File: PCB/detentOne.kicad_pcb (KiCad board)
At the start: 2 copper layers, 150 x 85 mm, 88 parts, among them J1 Conn_01x07, J2 Conn_01x03, SW1 SW_Push, SW2 SW_Push, SW3 SW_Push, SW4 SW_Push, SW5 SW_Push, SW6 SW_Push, SW7 C92589, SW8 C92589, U2 SGM2050XTRL20G/TR, U3 ESP32-S3-WROOM-1(N16R8), U4 TMC6300-LA-T_C5274455, U5 XY-GH1.25-7A61, U6 PCA9554ARGVR, U7 AS5047P-ATSM_C962063

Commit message: PCB schematic checked - ready to trace
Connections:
- C10 pad 1: VBAT -> 5V
- C12 pad 1: VBAT -> 5V
- C4 pad 2: /PowerManagement/5V -> 5V
- C9 pad 1: VBAT -> 5V
- D5 pad 1: USB_D+ -> USB_D+_UP
- D5 pad 3: USB_D- -> USB_D-_UP
- U2 pad 14: /PowerManagement/5V -> 5V
- U2 pad 15: /PowerManagement/5V -> 5V
- U2 pad 16: /PowerManagement/5V -> 5V
- U2 pad 17: /PowerManagement/5V -> 5V
- U4 pad 18: VBAT -> 5V
- USB1 pad 11: /PowerManagement/5V -> 5V
- USB1 pad 2: /PowerManagement/5V -> 5V
- USB1 pad 5: USB_D- -> USB_D-_UP
- USB1 pad 6: USB_D+ -> USB_D+_UP
- USB1 pad 7: USB_D- -> USB_D-_UP
- USB1 pad 8: USB_D+ -> USB_D+_UP
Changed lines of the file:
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@@
 	)
 	(net 0 "")
-	(net 1 "/PowerManagement/5V")
+	(net 1 "5V")
 	(net 2 "GND")
-	(net 3 "VBAT")
+	(net 3 "USB_D+_UP")
 	(net 4 "3V3")
 	(net 5 "Net-(U2-NR{slash}SS)")
@@
 	(net 95 "Net-(LED16-DOUT)")
 	(net 96 "unconnected-(LED17-DOUT-Pad2)")
+	(net 97 "USB_D-_UP")
 	(footprint "MountingHole:MountingHole_2.2mm_M2"
 		(layer "F.Cu")
@@
 			(layers "F.Cu" "F.Mask" "F.Paste")
 			(roundrect_rratio 0.25)
-			(net 3 "VBAT")
+			(net 1 "5V")
 			(pintype "passive")
 		)
@@
 			(layers "F.Cu" "F.Mask" "F.Paste")
 			(roundrect_rratio 0.25)
-			(net 3 "VBAT")
+			(net 1 "5V")
 			(pintype "passive")
 		)
@@
 			(size 0.55 1.1)
 			(layers "F.Cu" "F.Mask" "F.Paste")
-			(net 1 "/PowerManagement/5V")
+			(net 1 "5V")
 			(pinfunction "VBUS")
 			(pintype "unspecified")
@@
 			(size 0.3 1.1)
 			(layers "F.Cu" "F.Mask" "F.Paste")
-			(net 16 "USB_D-")
+			(net 97 "USB_D-_UP")
 			(pinfunction "DN2")
 			(pintype "unspecified")
@@
 			(size 0.3 1.1)
 			(layers "F.Cu" "F.Mask" "F.Paste")
-			(net 15 "USB_D+")
+			(net 3 "USB_D+_UP")
 			(pinfunction "DP1")
 			(pintype "unspecified")
@@
 			(size 0.3 1.1)
 			(layers "F.Cu" "F.Mask" "F.Paste")
-			(net 16 "USB_D-")
+			(net 97 "USB_D-_UP")
 			(pinfunction "DN1")
 			(pintype "unspecified")
@@
 			(size 0.3 1.1)
 			(layers "F.Cu" "F.Mask" "F.Paste")
-			(net 15 "USB_D+")
+			(net 3 "USB_D+_UP")
 			(pinfunction "DP2")
 			(pintype "unspecified")
@@
 			(size 0.55 1.1)
 			(layers "F.Cu" "F.Mask" "F.Paste")
-			(net 1 "/PowerManagement/5V")
+			(net 1 "5V")
 			(pinfunction "VBUS")
 			(pintype "unspecified")
@@
 			(size 0.53 1.07)
 			(layers "F.Cu" "F.Mask" "F.Paste")
-			(net 15 "USB_D+")
+			(net 3 "USB_D+_UP")
 			(pinfunction "1")
 			(pintype "input")
@@
 			(size 0.53 1.07)
 			(layers "F.Cu" "F.Mask" "F.Paste")
-			(net 16 "USB_D-")
+			(net 97 "USB_D-_UP")
 			(pinfunction "3")
 			(pintype "input")
@@
 			(layers "F.Cu" "F.Mask" "F.Paste")
 			(roundrect_rratio 0.25)
-			(net 1 "/PowerManagement/5V")
+			(net 1 "5V")
 			(pintype "passive")
 		)
@@
 			(size 0.66 0.2)
 			(layers "F.Cu" "F.Mask" "F.Paste")
-			(net 3 "VBAT")
+			(net 1 "5V")
 			(pinfunction "VS")
 			(pintype "unspecified")
@@
 			(size 0.28 0.8)
 			(layers "F.Cu" "F.Mask" "F.Paste")
-			(net 1 "/PowerManagement/5V")
+			(net 1 "5V")
 			(pinfunction "EN")
 			(pintype "unspecified")
@@
 			(size 0.28 0.8)
 			(layers "F.Cu" "F.Mask" "F.Paste")
-			(net 1 "/PowerManagement/5V")
+			(net 1 "5V")
 			(pinfunction "IN")
 			(pintype "unspecified")
@@
 			(size 0.8 0.28)
 			(layers "F.Cu" "F.Mask" "F.Paste")
-			(net 1 "/PowerManagement/5V")
+			(net 1 "5V")
 			(pinfunction "IN")
 			(pintype "unspecified")
@@
 			(size 0.8 0.28)
 			(layers "F.Cu" "F.Mask" "F.Paste")
-			(net 1 "/PowerManagement/5V")
+			(net 1 "5V")
 			(pinfunction "IN")
 			(pintype "unspecified")
@@
 			(layers "F.Cu" "F.Mask" "F.Paste")
 			(roundrect_rratio 0.25)
-			(net 3 "VBAT")
+			(net 1 "5V")
 			(pintype "passive")
 		)

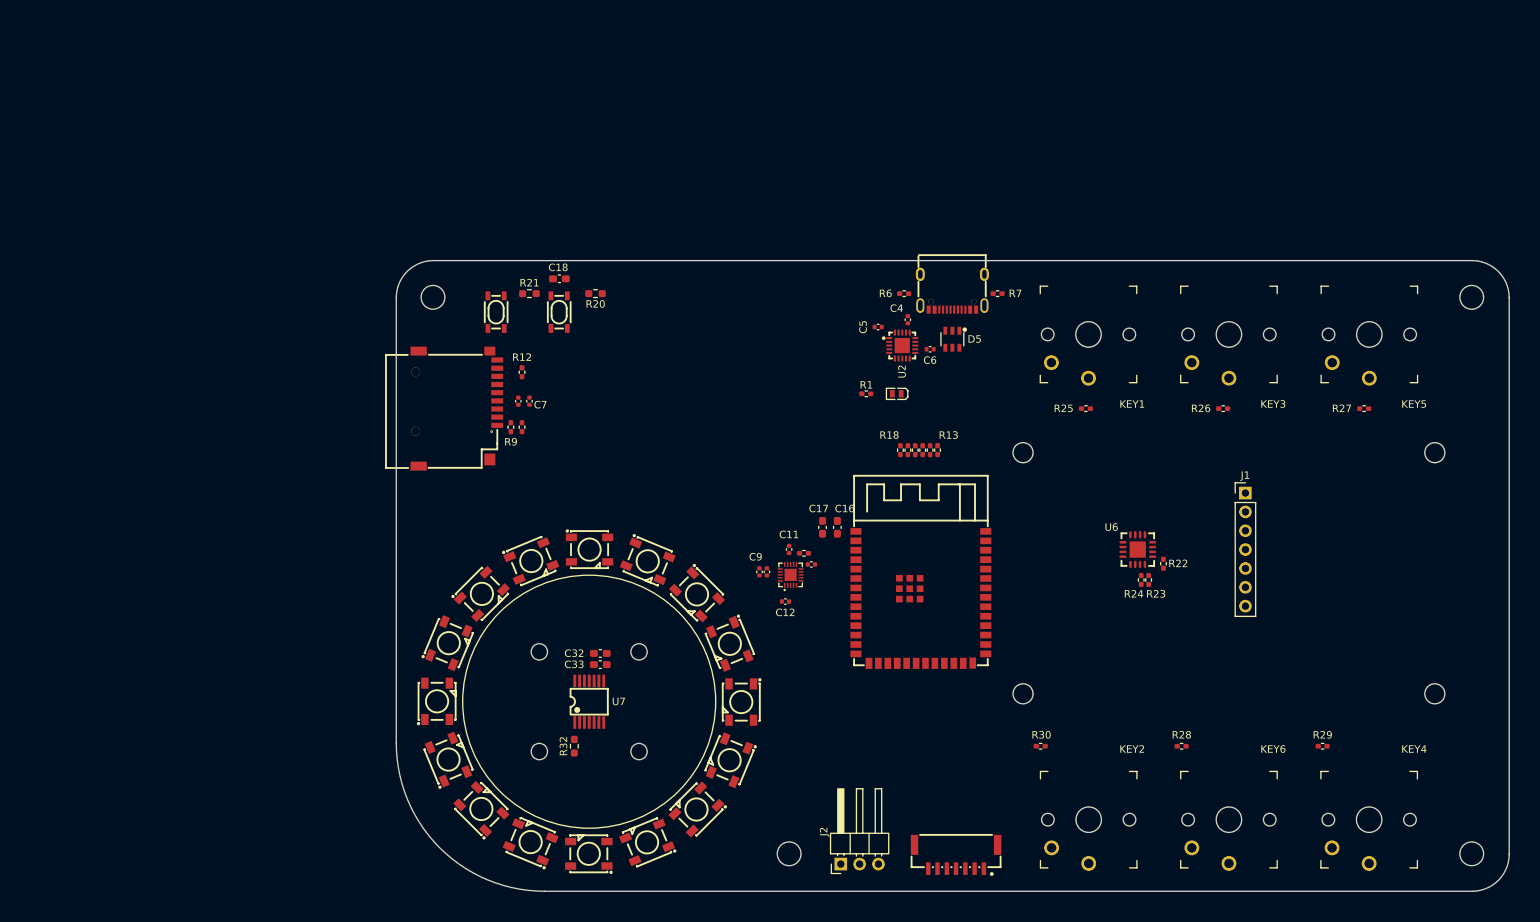
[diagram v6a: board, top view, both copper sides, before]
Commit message: encoder and spi left to trace
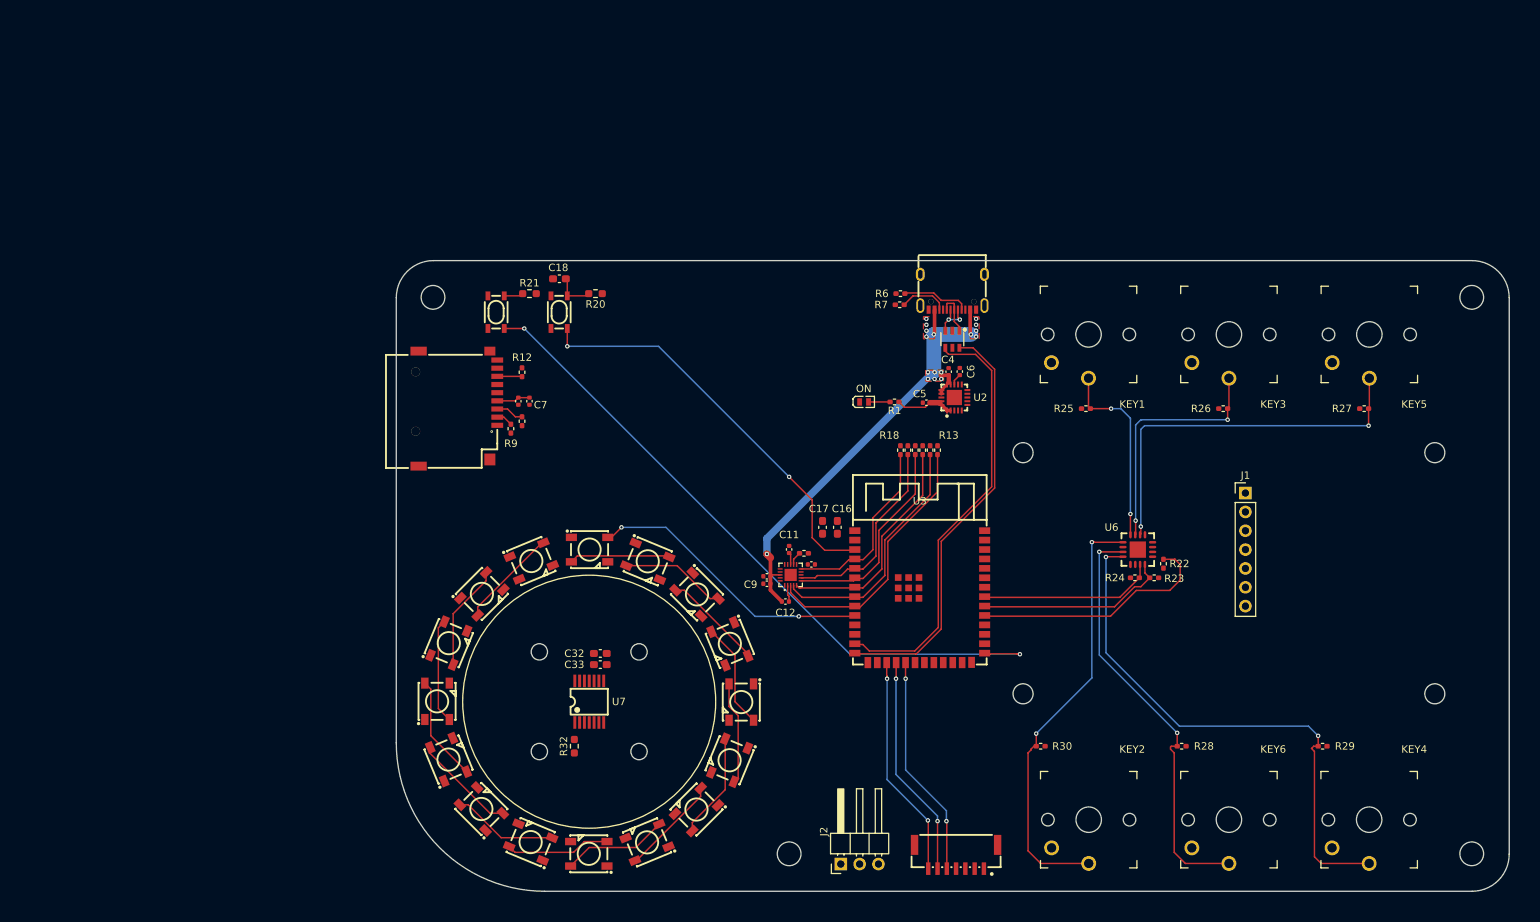
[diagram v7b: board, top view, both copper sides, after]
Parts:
- moved R7 13.3 mm to (151.9, 57.5), turned to 180 degrees
- moved C5 12.1 mm to (155.5, 70.7)
- moved U2 9.91 mm to (159.3, 70.0), turned to 0 degrees
- moved C4 8.90 mm to (158.5, 66.5)
- moved C6 5.00 mm to (160.0, 66.5), turned to -90 degrees
- moved LED1 4.53 mm to (147.1, 70.6), turned to 0 degrees
- moved R1 3.96 mm to (151.2, 70.6), turned to 180 degrees
- moved C9 1.89 mm to (134.0, 95.1), turned to 180 degrees
- moved R24 0.90 mm to (183.6, 94.3), turned to 180 degrees
- moved R23 0.81 mm to (186.2, 94.3), turned to 0 degrees
- moved R10 0.80 mm to (101.0, 73.2)
- moved C10 0.60 mm to (134.0, 94.1), turned to 180 degrees
- moved R6 0.50 mm to (152.0, 56.0)
- moved R9 0.20 mm to (99.5, 74.2)
- moved U3 0.18 mm to (154.6, 96.8)
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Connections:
- U3 pad 10: A_OUT -> NEOPIXEL_DIN
- U3 pad 11: B_OUT -> A_OUT
- U3 pad 12: CURRENT_SENSE -> B_OUT
- U3 pad 17: OLED_DC -> OLED_RST
- U3 pad 18: OLED_RST -> OLED_DC
- U3 pad 19: MOSI -> OLED_CS
- U3 pad 20: SCK -> MOSI
- U3 pad 21: MISO -> SCK
- U3 pad 22: NEOPIXEL_DIN -> MISO
- U3 pad 35: OLED_CS -> unconnected-(U3-IO42-Pad35)
- U3 pad 38: CHG -> unconnected-(U3-IO2-Pad38)
- U3 pad 39: CE -> unconnected-(U3-IO1-Pad39)
- U3 pad 40: unconnected-(U3-GND-Pad40) -> GND
- U3 pad 41: unconnected-(U3-GND-Pad41) -> GND
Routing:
- net BOOT: track 0.00 -> 94.9 mm, vias 0 -> 2
- net KEY4: track 0.00 -> 73.4 mm, vias 0 -> 2
- net 5V: track 0.00 -> 65.3 mm, vias 0 -> 17
- net EN: track 0.00 -> 61.1 mm, vias 0 -> 2
- net KEY2: track 0.00 -> 58.4 mm, vias 0 -> 2
- net USB_D-: track 0.00 -> 58.2 mm
- net KEY6: track 0.00 -> 57.1 mm, vias 0 -> 2
- net USB_D+: track 0.00 -> 56.8 mm
- net KEY5: track 0.00 -> 51.6 mm, vias 0 -> 2
- net NEOPIXEL_DIN: track 0.00 -> 38.9 mm, vias 0 -> 2
- net UH: track 0.00 -> 36.0 mm
- net VH: track 0.00 -> 33.3 mm
- net KEY3: track 0.00 -> 33.2 mm, vias 0 -> 2
- net SDA: track 0.00 -> 32.9 mm
- net WH: track 0.00 -> 30.4 mm
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- added copper zone on B.Cu, net 5V
- added copper zone on F.Cu, net 5V
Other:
- copper layers 2 -> 4
- board text added: "Don't run traces under Antenna!"
- board text added: "Replace with WROOM-1U Variant"
- board text added: "Width: 0.2mm Spacing: 0.1mm"
- board text removed: "Remove Lipo Functionality!"

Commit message: PCB traced
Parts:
- J1: footprint Connector_PinHeader_2.54mm:PinHeader_1x07_P2.54mm_Vertical -> Connector_PinHeader_2.54mm:PinHeader_1x07_P2.54mm_Horizontal
- moved J2 64.3 mm to (130.7, 69.9), turned to -90 degrees
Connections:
- U3 pad 20: MOSI -> MISO
- U3 pad 22: MISO -> MOSI
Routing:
- net SCK: track 0.00 -> 208.2 mm, vias 0 -> 4
- net MOSI: track 3.77 -> 186.9 mm
- net MISO: track 3.36 -> 115.2 mm, vias 0 -> 2
- net 3V3: track 12.3 -> 120.8 mm, vias 0 -> 52
- net SD_CS: track 2.23 -> 102.2 mm, vias 0 -> 4
- net ENCODER_CS: track 0.00 -> 62.5 mm, vias 0 -> 5
- net OLED_RST: track 30.1 -> 90.6 mm, vias 2 -> 3
- net OLED_DC: track 30.1 -> 86.3 mm, vias 2 -> 5
- net OLED_CS: track 30.1 -> 84.9 mm, vias 2 -> 3
- net GND: track 0.00 -> 52.1 mm, vias 0 -> 21
- net B_OUT: track 0.00 -> 41.2 mm, vias 0 -> 2
- net A_OUT: track 0.00 -> 40.6 mm, vias 0 -> 2
- net W: track 0.00 -> 33.6 mm
- net V: track 0.00 -> 30.2 mm
- net U: track 0.00 -> 27.4 mm
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- added copper zone on In2.Cu, net 3V3
- added copper zone on B.Cu, net GND
- added copper zone on F.Cu, net GND
- added copper zone on In1.Cu, net GND
